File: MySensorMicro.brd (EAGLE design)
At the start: 17.7 x 30.5 mm, 21 parts, among them IC1 MEGA328P-AU, IC2 AT25DF512C-SSHN-B, IC3 SI7021, IC4 ATSHA204A, Q1 32768hz

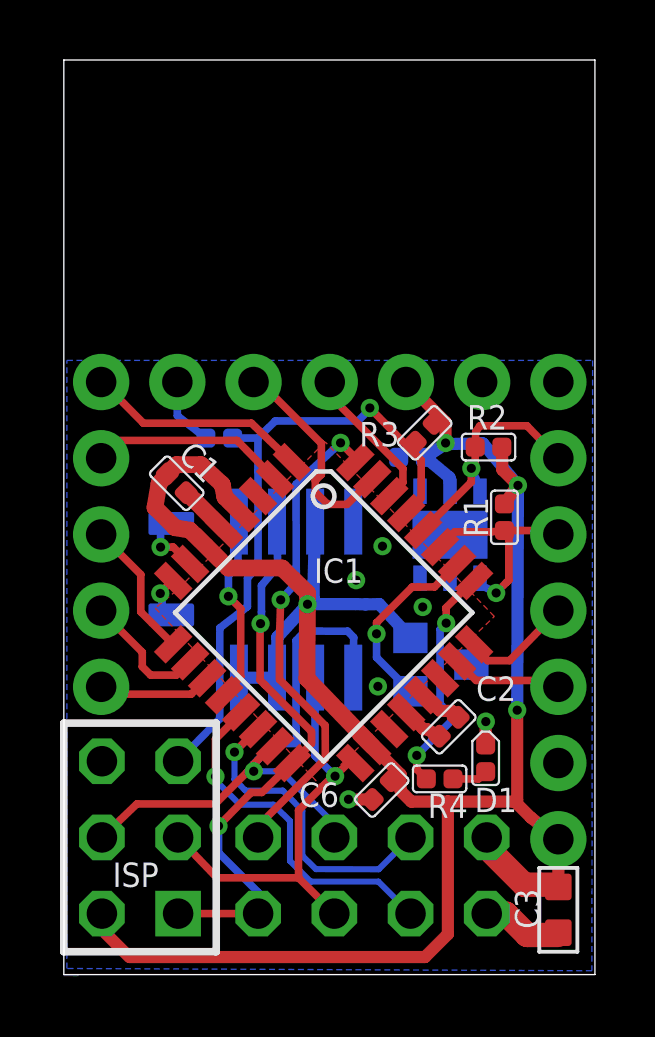
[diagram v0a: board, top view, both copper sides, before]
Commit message: Updated with pullup on both CSN on NRF module, and CE on external flash
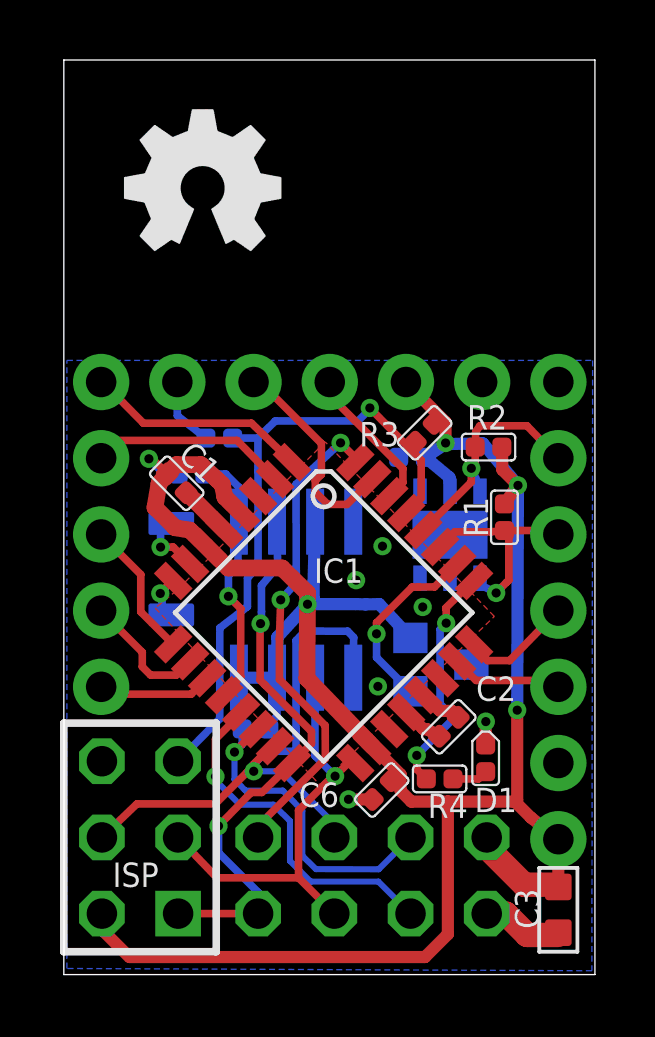
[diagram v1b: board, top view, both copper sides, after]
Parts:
- added R5, R6: 4k7, Discrete:R0402
- JP2, JP4, JP5: value (none) -> N/M
- JP3: value AVR-ISP-6VERT -> N/M
- Q1: value 32768hz -> N/M
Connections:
- net D10: now also R6.1
- net D8: now also R5.1
- net V+: now also R5.2, R6.2
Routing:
- net V+: track 78.7 -> 82.6 mm, vias 4 -> 5
- net D8: track 6.35 -> 8.81 mm
- net D10: track 10.4 -> 11.3 mm
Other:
- board text removed: "/home/thomas/Hentninger/pcb(2).BMP"

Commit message: Updated component values on R5/R6
Fix error > Board and schematic are not consistent! No
forward-/backannotation will be performed!
Changes are done using Eagle 7.3.0
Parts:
- R5, R6: value 4k7 -> 56k
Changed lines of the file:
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@@
 <?xml version="1.0" encoding="utf-8"?>
 <!DOCTYPE eagle SYSTEM "eagle.dtd">
-<eagle version="7.2.0">
+<eagle version="7.3.0">
 <drawing>
 <settings>
@@
 <attribute name="VALUE" x="11.932921875" y="8.681721875" size="0.635" layer="28" ratio="10" rot="MR90"/>
 </element>
-<element name="R5" library="Discrete" package="R0402" value="4k7" x="4.258303125" y="16.686525" rot="MR90"/>
-<element name="R6" library="Discrete" package="R0402" value="4k7" x="6.391915625" y="8.1876875" rot="MR270"/>
+<element name="R5" library="Discrete" package="R0402" value="56k" x="4.258303125" y="16.686525" rot="MR90"/>
+<element name="R6" library="Discrete" package="R0402" value="56k" x="6.391915625" y="8.1876875" rot="MR270"/>
 </elements>
 <signals>
